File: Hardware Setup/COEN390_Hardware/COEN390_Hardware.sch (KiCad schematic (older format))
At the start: 1 part

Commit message: Fix to the Hardware schematic
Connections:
- net labels added: RelaySwitch
- wire segments 30 -> 28
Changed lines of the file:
@@
 $EndComp
-Wire Wire Line
-	1850 2850 2700 2850
-Wire Wire Line
-	2700 2850 2700 1350
 Wire Wire Line
 	1850 2450 2300 2450
@@
 F0 "Fan Configuration" 50
 F1 "FanConfig.sch" 50
-F2 "5V" I L 9100 2550 50
+F2 "RelaySwitch" I L 9100 2550 50
 F3 "GND" I L 9100 2850 50
 $EndSheet
@@
 Wire Wire Line
 	10000 1200 10400 1200
-$Comp
-L power:+5V #PWR?
-U 1 1 604B3AF8
-P 8750 2250
-F 0 "#PWR?" H 8750 2100 50  0001 C CNN
-F 1 "+5V" H 8765 2423 50  0000 C CNN
-F 2 "" H 8750 2250 50  0001 C CNN
-F 3 "" H 8750 2250 50  0001 C CNN
-	1    8750 2250
-	1    0    0    -1
-$EndComp
 $Comp
 L power:+5V #PWR?
@@
 $EndComp
 Wire Wire Line
-	8750 2250 8750 2550
-Wire Wire Line
 	8750 2550 9100 2550
 Wire Wire Line
@@
 Wire Wire Line
 	10000 4200 10250 4200
+Text GLabel 2300 4950 2    50   Output ~ 0
+RelaySwitch
+Wire Wire Line
+	2300 4950 1850 4950
+Text GLabel 8250 2550 2    50   Output ~ 0
+RelaySwitch
 $EndSCHEMATC

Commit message: Edited Arduino set up
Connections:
- net labels added: AirSensorSwitch
- wire segments 28 -> 30
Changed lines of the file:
@@
 F1 "MQ-135.sch" 50
 F2 "5V" I L 9100 1050 50
-F3 "Analog_Out" O R 10000 1200 50
+F3 "Analog_Out" O R 10000 1350 50
 F4 "GND" I L 9100 1350 50
+F5 "AirSensorSwitch" I L 9100 1200 50
 $EndSheet
 Wire Wire Line
@@
 Wire Wire Line
 	2300 3200 1850 3200
-Text GLabel 10400 1200 2    50   Output ~ 0
+Text GLabel 10400 1350 2    50   Output ~ 0
 AirQualityValue
 $Sheet
@@
 Wire Wire Line
 	8750 1350 8750 1550
-Wire Wire Line
-	10000 1200 10400 1200
 $Comp
 L power:+5V #PWR?
@@
 Text GLabel 8250 2550 2    50   Output ~ 0
 RelaySwitch
+Wire Wire Line
+	10400 1350 10000 1350
+Wire Wire Line
+	9100 1200 8750 1200
+Text GLabel 2300 5150 2    50   Output ~ 0
+AirSensorSwitch
+Wire Wire Line
+	1850 5150 2300 5150
+Text GLabel 8750 1200 0    50   Input ~ 0
+AirSensorSwitch
 $EndSCHEMATC

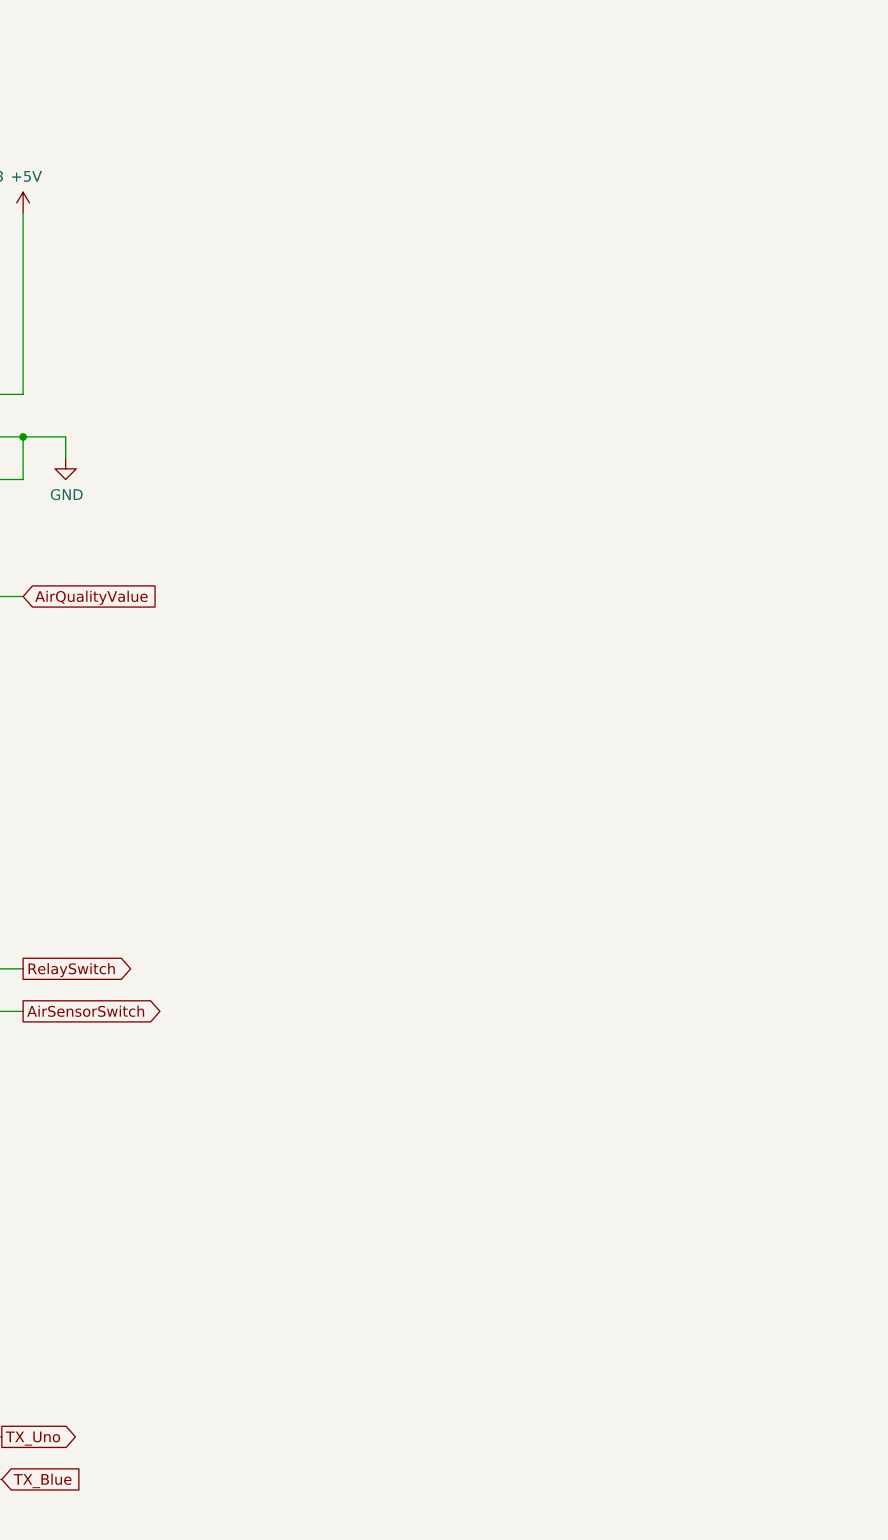
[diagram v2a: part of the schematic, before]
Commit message: Added the humidifier arduino and app
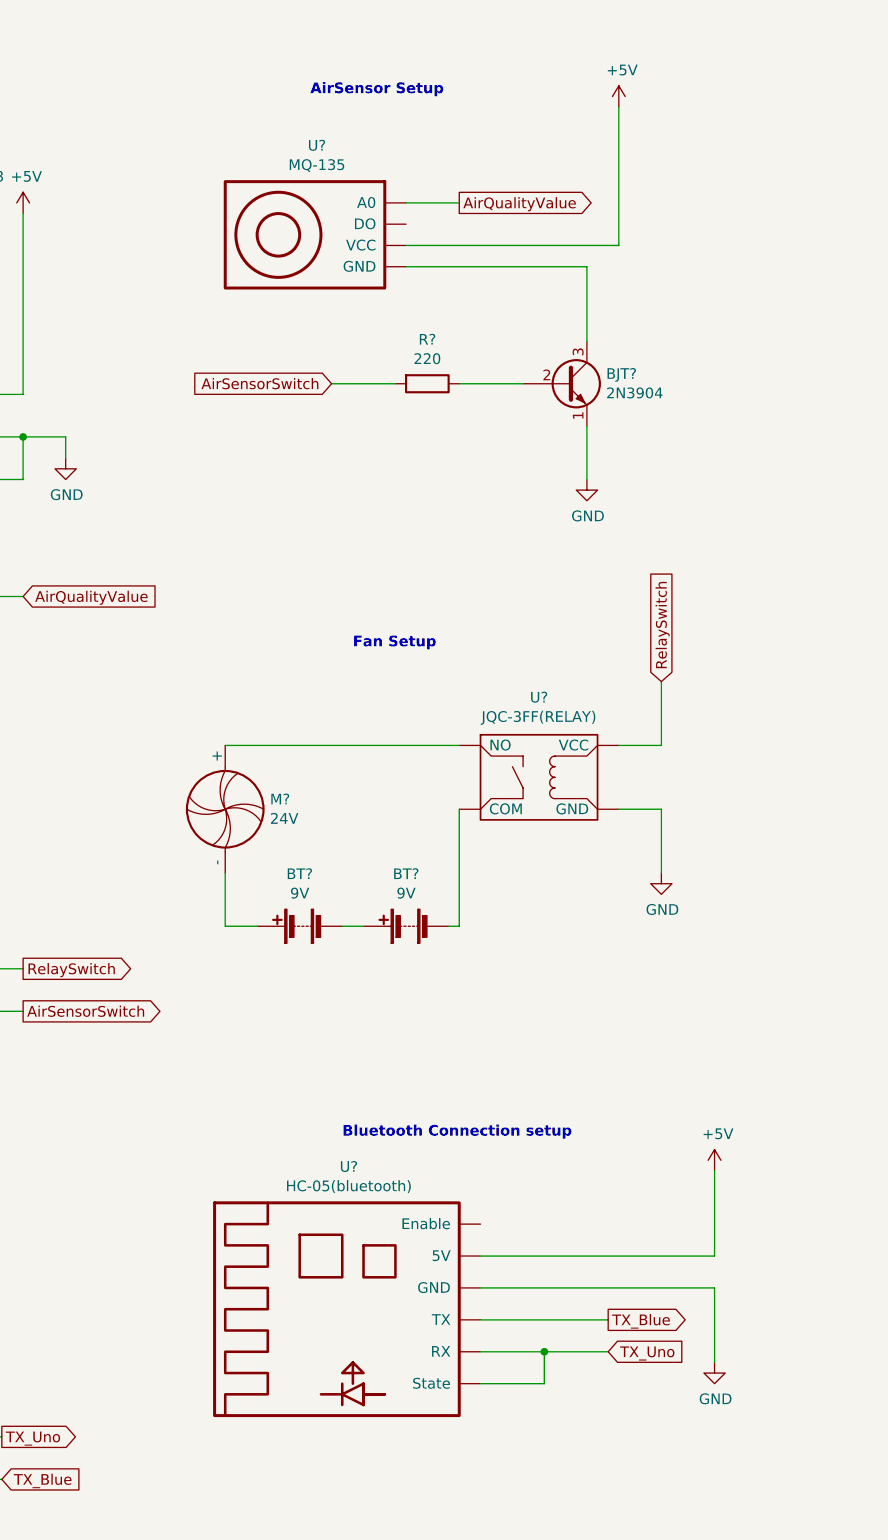
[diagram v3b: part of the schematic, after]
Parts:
- added BJT?: 2N3904, Package_TO_SOT_THT:TO-92_Inline, symbol Transistor_BJT:2N3904
- added BT? (x2): 9V, symbol Device:Battery
- added M?: 24V, symbol Motor:Fan_ALT
- added R?: 220, symbol Device:R
- added U?: MQ-135, symbol COEN390_Hardware:MQ-135
- added U?: JQC-3FF(RELAY), symbol COEN390_Hardware:JQC-3FF(RELAY)
- added U?: HC-05(bluetooth), symbol COEN390_Hardware:HC-05(bluetooth)
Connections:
- wire segments 30 -> 57
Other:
- note added: "AirSensor Setup"
- note added: "Bluetooth Connection setup"
- note added: "Fan Setup"
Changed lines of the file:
@@
 Text GLabel 8750 1200 0    50   Input ~ 0
 AirSensorSwitch
+$Comp
+L COEN390_Hardware:MQ-135 U?
+U 1 1 6060D5EE
+P 4000 1500
+AR Path="/604A3244/6060D5EE" Ref="U?"  Part="1"
+AR Path="/6060D5EE" Ref="U?"  Part="1"
+F 0 "U?" H 3681 1919 50  0000 C CNN
+F 1 "MQ-135" H 3681 1828 50  0000 C CNN
+F 2 "" H 4000 1500 50  0001 C CNN
+F 3 "" H 4000 1500 50  0001 C CNN
+	1    4000 1500
+	1    0    0    -1
+$EndComp
+Wire Wire Line
+	5100 900  5100 1550
+Wire Wire Line
+	4100 1650 4950 1650
+Wire Wire Line
+	4100 1350 4350 1350
+$Comp
+L Transistor_BJT:2N3904 BJT?
+U 1 1 6060D5FC
+P 4850 2200
+AR Path="/604A3244/6060D5FC" Ref="BJT?"  Part="1"
+AR Path="/6060D5FC" Ref="BJT?"  Part="1"
+F 0 "BJT?" H 5040 2246 50  0000 L CNN
+F 1 "2N3904" H 5040 2155 50  0000 L CNN
+F 2 "Package_TO_SOT_THT:TO-92_Inline" H 5050 2125 50  0001 L CIN
+F 3 "https://www.onsemi.com/pub/Collateral/2N3903-D.PDF" H 4850 2200 50  0001 L CNN
+	1    4850 2200
+	1    0    0    -1
+$EndComp
+Wire Wire Line
+	4950 2650 4950 2400
+$Comp
+L Device:R R?
+U 1 1 6060D604
+P 4200 2200
+AR Path="/604A3244/6060D604" Ref="R?"  Part="1"
+AR Path="/6060D604" Ref="R?"  Part="1"
+F 0 "R?" V 3993 2200 50  0000 C CNN
+F 1 "220" V 4084 2200 50  0000 C CNN
+F 2 "" V 4130 2200 50  0001 C CNN
+F 3 "~" H 4200 2200 50  0001 C CNN
+	1    4200 2200
+	0    1    1    0
+$EndComp
+Wire Wire Line
+	4350 2200 4650 2200
+Wire Wire Line
+	4050 2200 3750 2200
+Wire Wire Line
+	4950 1650 4950 2000
+Text GLabel 3750 2200 0    50   Input ~ 0
+AirSensorSwitch
+$Comp
+L power:+5V #PWR?
+U 1 1 6062C9D2
+P 5100 900
+F 0 "#PWR?" H 5100 750 50  0001 C CNN
+F 1 "+5V" H 5115 1073 50  0000 C CNN
+F 2 "" H 5100 900 50  0001 C CNN
+F 3 "" H 5100 900 50  0001 C CNN
+	1    5100 900
+	1    0    0    -1
+$EndComp
+Text Notes 3650 850  0    50   ~ 10
+AirSensor Setup
+Text Notes 3850 3450 0    50   ~ 10
+Fan Setup
+$Comp
+L power:GND #PWR?
+U 1 1 60626E83
+P 5300 4500
+F 0 "#PWR?" H 5300 4250 50  0001 C CNN
+F 1 "GND" H 5305 4327 50  0000 C CNN
+F 2 "" H 5300 4500 50  0001 C CNN
+F 3 "" H 5300 4500 50  0001 C CNN
+	1    5300 4500
+	1    0    0    -1
+$EndComp
+Text GLabel 5300 3600 1    50   Input ~ 0
+RelaySwitch
+Wire Wire Line
+	5100 4200 5300 4200
+Wire Wire Line
+	5300 4200 5300 4500
+Wire Wire Line
+	5300 3900 5300 3600
+Wire Wire Line
+	5100 3900 5300 3900
+Wire Wire Line
+	4350 4750 4300 4750
+Wire Wire Line
+	3900 4750 3800 4750
+Wire Wire Line
+	3400 4750 3250 4750
+$Comp
+L Device:Battery BT?
+U 1 1 606188CC
+P 4100 4750
+AR Path="/604AB21D/606188CC" Ref="BT?"  Part="1"
+AR Path="/606188CC" Ref="BT?"  Part="1"
+F 0 "BT?" V 4345 4750 50  0000 C CNN
+F 1 "9V" V 4254 4750 50  0000 C CNN
+F 2 "" V 4100 4810 50  0001 C CNN
+F 3 "~" V 4100 4810 50  0001 C CNN
+	1    4100 4750
+	0    -1   -1   0
+$EndComp
+Wire Wire Line
+	4350 4750 4350 4200
+Wire Wire Line
+	3250 4500 3250 4750
+$Comp
+L Device:Battery BT?
+U 1 1 606188C4
+P 3600 4750
+AR Path="/604AB21D/606188C4" Ref="BT?"  Part="1"
+AR Path="/606188C4" Ref="BT?"  Part="1"
+F 0 "BT?" V 3845 4750 50  0000 C CNN
+F 1 "9V" V 3754 4750 50  0000 C CNN
+F 2 "" V 3600 4810 50  0001 C CNN
+F 3 "~" V 3600 4810 50  0001 C CNN
+	1    3600 4750
+	0    -1   -1   0
+$EndComp
+Wire Wire Line
+	3250 3900 4350 3900
+$Comp
+L COEN390_Hardware:JQC-3FF(RELAY) U?
+U 1 1 606188BD
+P 4700 4050
+AR Path="/604AB21D/606188BD" Ref="U?"  Part="1"
+AR Path="/606188BD" Ref="U?"  Part="1"
+F 0 "U?" H 4725 4425 50  0000 C CNN
+F 1 "JQC-3FF(RELAY)" H 4725 4334 50  0000 C CNN
+F 2 "" H 4750 3900 50  0001 C CNN
+F 3 "" H 4750 3900 50  0001 C CNN
+	1    4700 4050
+	1    0    0    -1
+$EndComp
+$Comp
+L Motor:Fan_ALT M?
+U 1 1 606188B7
+P 3250 4200
+AR Path="/604AB21D/606188B7" Ref="M?"  Part="1"
+AR Path="/606188B7" Ref="M?"  Part="1"
+F 0 "M?" H 3460 4246 50  0000 L CNN
+F 1 "24V" H 3460 4155 50  0000 L CNN
+F 2 "" H 3250 4150 50  0001 C CNN
+F 3 "~" H 3250 4150 50  0001 C CNN
+	1    3250 4200
+	1    0    0    -1
+$EndComp
+Text Notes 3800 5750 0    50   ~ 10
+Bluetooth Connection setup
+$Comp
+L power:GND #PWR?
+U 1 1 60630A39
+P 5550 6800
+F 0 "#PWR?" H 5550 6550 50  0001 C CNN
+F 1 "GND" H 5555 6627 50  0000 C CNN
+F 2 "" H 5550 6800 50  0001 C CNN
+F 3 "" H 5550 6800 50  0001 C CNN
+	1    5550 6800
+	1    0    0    -1
+$EndComp
+$Comp
+L power:+5V #PWR?
+U 1 1 6062EA0C
+P 5550 5900
+F 0 "#PWR?" H 5550 5750 50  0001 C CNN
+F 1 "+5V" H 5565 6073 50  0000 C CNN
+F 2 "" H 5550 5900 50  0001 C CNN
+F 3 "" H 5550 5900 50  0001 C CNN
+	1    5550 5900
+	1    0    0    -1
+$EndComp
+Wire Wire Line
+	4750 6750 4450 6750
+Connection ~ 4750 6750
+Wire Wire Line
+	4750 6900 4750 6750
+Wire Wire Line
+	4450 6900 4750 6900
+Wire Wire Line
+	5550 5900 5550 6300
+Wire Wire Line
+	5050 6600 4450 6600
+Wire Wire Line
+	5050 6750 4750 6750
+$Comp
+L COEN390_Hardware:HC-05(bluetooth) U?
+U 1 1 6061A274
+P 4350 6500
+AR Path="/604B18C9/6061A274" Ref="U?"  Part="1"
+AR Path="/6061A274" Ref="U?"  Part="1"
+F 0 "U?" H 3831 7119 50  0000 C CNN
+F 1 "HC-05(bluetooth)" H 3831 7028 50  0000 C CNN
+F 2 "" H 4350 6350 50  0001 C CNN
+F 3 "" H 4350 6350 50  0001 C CNN
+	1    4350 6500
+	1    0    0    -1
+$EndComp
+Wire Wire Line
+	4450 6300 5550 6300
+Wire Wire Line
+	4450 6450 5550 6450
+Wire Wire Line
+	5550 6450 5550 6800
+$Comp
+L power:GND #PWR?
+U 1 1 6065B9CA
+P 4950 2650
+F 0 "#PWR?" H 4950 2400 50  0001 C CNN
+F 1 "GND" H 4955 2477 50  0000 C CNN
+F 2 "" H 4950 2650 50  0001 C CNN
+F 3 "" H 4950 2650 50  0001 C CNN
+	1    4950 2650
+	1    0    0    -1
+$EndComp
+Text GLabel 4350 1350 2    50   Output ~ 0
+AirQualityValue
+Wire Wire Line
+	4100 1550 5100 1550
+Text GLabel 5050 6750 2    50   Input ~ 0
+TX_Uno
+Text GLabel 5050 6600 2    50   Output ~ 0
+TX_Blue
 $EndSCHEMATC
